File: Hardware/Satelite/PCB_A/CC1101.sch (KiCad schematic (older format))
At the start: 18 parts, among them U2 CC1101RGP, U3 0915BM15A0001E, Y1 26 MHz

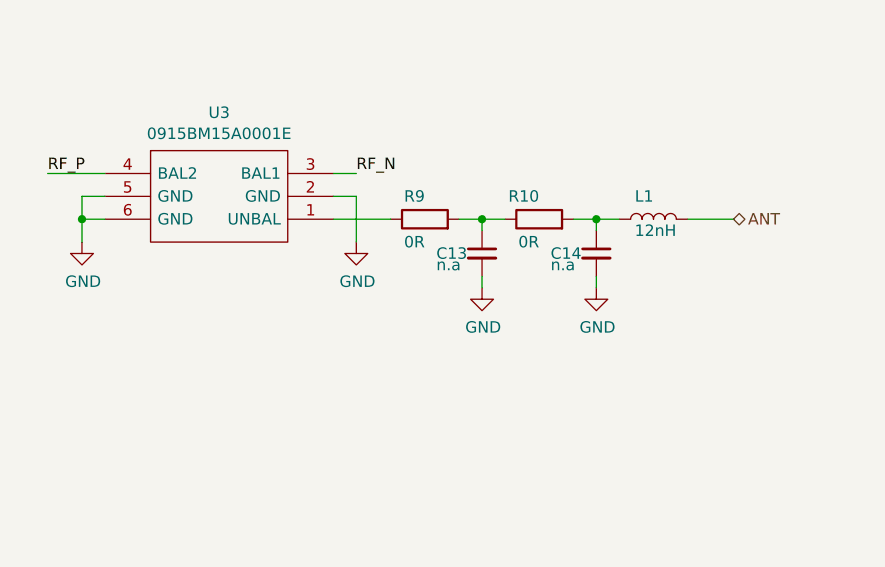
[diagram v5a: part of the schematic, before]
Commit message: Agregado capacitor de bloqueo para el Balun 0896BM15A0001E
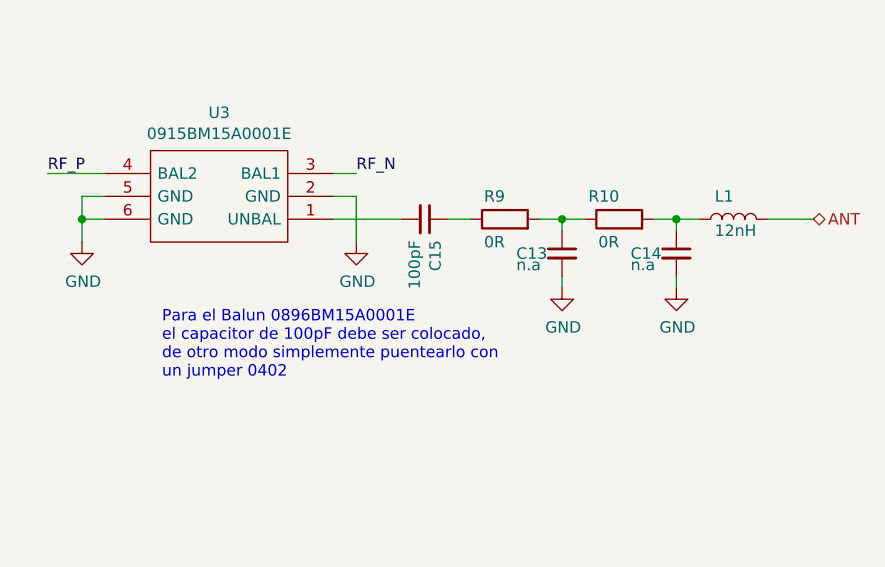
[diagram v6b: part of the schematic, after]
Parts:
- added C15: 100pF, Capacitor_SMD:C_0402_1005Metric, symbol Device:C_Small
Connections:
- net at R9.1: now also C15.1; no longer U3.1 (UNBAL)
- new net: C15.2, U3.1 (UNBAL)
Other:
- note added: "Para el Balun 0896BM15A0001E\nel capacitor de 100pF debe ser colocado,\nde otro modo simplemente puentearlo con\nun jumper 0402"
- moved on the sheet: C13, C14, L1, R10, R9
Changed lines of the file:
@@
 Wire Wire Line
 	3400 4600 3400 4450
-Text HLabel 9300 3400 2    50   BiDi ~ 0
+Text HLabel 9650 3400 2    50   BiDi ~ 0
 ANT
 $Comp
 L Device:C_Small C?
 U 1 1 5BCB61AE
-P 8200 3550
+P 8550 3550
 AR Path="/5B9A8077/5BCB61AE" Ref="C?"  Part="1"
 AR Path="/5BA17F9C/5BCB61AE" Ref="C13"  Part="1"
-F 0 "C13" H 8000 3550 50  0000 L CNN
-F 1 "n.a" H 8000 3500 50  0000 L CNN
-F 2 "Capacitor_SMD:C_0402_1005Metric" H 8200 3550 50  0001 C CNN
-F 3 "~" H 8200 3550 50  0001 C CNN
-	1    8200 3550
+F 0 "C13" H 8350 3550 50  0000 L CNN
+F 1 "n.a" H 8350 3500 50  0000 L CNN
+F 2 "Capacitor_SMD:C_0402_1005Metric" H 8550 3550 50  0001 C CNN
+F 3 "~" H 8550 3550 50  0001 C CNN
+	1    8550 3550
 	1    0    0    -1
 $EndComp
@@
 L Device:R R?
 U 1 1 5BCB61B6
-P 7950 3400
+P 8300 3400
 AR Path="/5B9A8077/5BCB61B6" Ref="R?"  Part="1"
 AR Path="/5BA17F9C/5BCB61B6" Ref="R9"  Part="1"
-F 0 "R9" V 8050 3400 50  0000 L CNN
-F 1 "0R" V 7850 3400 50  0000 L CNN
-F 2 "Resistor_SMD:R_0402_1005Metric" V 7880 3400 50  0001 C CNN
-F 3 "~" H 7950 3400 50  0001 C CNN
-F 4 "RC0402JR-070RL" V 7950 3400 50  0001 C CNN "Manufacturer Part Number"
-	1    7950 3400
+F 0 "R9" V 8400 3400 50  0000 L CNN
+F 1 "0R" V 8200 3400 50  0000 L CNN
+F 2 "Resistor_SMD:R_0402_1005Metric" V 8230 3400 50  0001 C CNN
+F 3 "~" H 8300 3400 50  0001 C CNN
+F 4 "RC0402JR-070RL" V 8300 3400 50  0001 C CNN "Manufacturer Part Number"
+	1    8300 3400
 	0    -1   -1   0
 $EndComp
@@
 L Device:L L?
 U 1 1 5BCB61BE
-P 8950 3400
+P 9300 3400
 AR Path="/5B9A8077/5BCB61BE" Ref="L?"  Part="1"
 AR Path="/5BA17F9C/5BCB61BE" Ref="L1"  Part="1"
-F 0 "L1" V 9050 3400 50  0000 L CNN
-F 1 "12nH" V 8900 3300 50  0000 L CNN
-F 2 "Inductor_SMD:L_0402_1005Metric" H 8950 3400 50  0001 C CNN
-F 3 "https://www.mouser.com/datasheet/2/611/jti-cat-rf-ind-844822.pdf" H 8950 3400 50  0001 C CNN
-F 4 "L-07C12NJV6" V 8950 3400 50  0001 C CNN "Manufacturer Part Number"
-	1    8950 3400
+F 0 "L1" V 9400 3400 50  0000 L CNN
+F 1 "12nH" V 9250 3300 50  0000 L CNN
+F 2 "Inductor_SMD:L_0402_1005Metric" H 9300 3400 50  0001 C CNN
+F 3 "https://www.mouser.com/datasheet/2/611/jti-cat-rf-ind-844822.pdf" H 9300 3400 50  0001 C CNN
+F 4 "L-07C12NJV6" V 9300 3400 50  0001 C CNN "Manufacturer Part Number"
+	1    9300 3400
 	0    -1   -1   0
 $EndComp
@@
 L Device:C_Small C?
 U 1 1 5BCB6272
-P 8700 3550
+P 9050 3550
 AR Path="/5B9A8077/5BCB6272" Ref="C?"  Part="1"
 AR Path="/5BA17F9C/5BCB6272" Ref="C14"  Part="1"
-F 0 "C14" H 8500 3550 50  0000 L CNN
-F 1 "n.a" H 8500 3500 50  0000 L CNN
-F 2 "Capacitor_SMD:C_0402_1005Metric" H 8700 3550 50  0001 C CNN
-F 3 "~" H 8700 3550 50  0001 C CNN
-	1    8700 3550
-	1    0    0    -1
-$EndComp
-Wire Wire Line
-	8100 3400 8200 3400
-Wire Wire Line
-	8200 3450 8200 3400
-Connection ~ 8200 3400
-Wire Wire Line
-	8200 3400 8300 3400
-Wire Wire Line
-	8600 3400 8700 3400
-Wire Wire Line
-	8700 3450 8700 3400
-Connection ~ 8700 3400
-Wire Wire Line
-	8700 3400 8800 3400
-Wire Wire Line
-	7550 3400 7800 3400
+F 0 "C14" H 8850 3550 50  0000 L CNN
+F 1 "n.a" H 8850 3500 50  0000 L CNN
+F 2 "Capacitor_SMD:C_0402_1005Metric" H 9050 3550 50  0001 C CNN
+F 3 "~" H 9050 3550 50  0001 C CNN
+	1    9050 3550
+	1    0    0    -1
+$EndComp
+Wire Wire Line
+	8450 3400 8550 3400
+Wire Wire Line
+	8550 3450 8550 3400
+Connection ~ 8550 3400
+Wire Wire Line
+	8550 3400 8650 3400
+Wire Wire Line
+	8950 3400 9050 3400
+Wire Wire Line
+	9050 3450 9050 3400
+Connection ~ 9050 3400
+Wire Wire Line
+	9050 3400 9150 3400
 $Comp
 L power:GND #PWR?
 U 1 1 5BCB6282
-P 8200 3700
+P 8550 3700
 AR Path="/5B9A8077/5BCB6282" Ref="#PWR?"  Part="1"
 AR Path="/5BA17F9C/5BCB6282" Ref="#PWR044"  Part="1"
-F 0 "#PWR044" H 8200 3450 50  0001 C CNN
-F 1 "GND" H 8205 3527 50  0000 C CNN
-F 2 "" H 8200 3700 50  0001 C CNN
-F 3 "" H 8200 3700 50  0001 C CNN
-	1    8200 3700
+F 0 "#PWR044" H 8550 3450 50  0001 C CNN
+F 1 "GND" H 8555 3527 50  0000 C CNN
+F 2 "" H 8550 3700 50  0001 C CNN
+F 3 "" H 8550 3700 50  0001 C CNN
+	1    8550 3700
 	1    0    0    -1
 $EndComp
@@
 L power:GND #PWR?
 U 1 1 5BCB6288
-P 8700 3700
+P 9050 3700
 AR Path="/5B9A8077/5BCB6288" Ref="#PWR?"  Part="1"
 AR Path="/5BA17F9C/5BCB6288" Ref="#PWR045"  Part="1"
-F 0 "#PWR045" H 8700 3450 50  0001 C CNN
-F 1 "GND" H 8705 3527 50  0000 C CNN
-F 2 "" H 8700 3700 50  0001 C CNN
-F 3 "" H 8700 3700 50  0001 C CNN
-	1    8700 3700
-	1    0    0    -1
-$EndComp
-Wire Wire Line
-	8200 3650 8200 3700
-Wire Wire Line
-	8700 3650 8700 3700
+F 0 "#PWR045" H 9050 3450 50  0001 C CNN
+F 1 "GND" H 9055 3527 50  0000 C CNN
+F 2 "" H 9050 3700 50  0001 C CNN
+F 3 "" H 9050 3700 50  0001 C CNN
+	1    9050 3700
+	1    0    0    -1
+$EndComp
+Wire Wire Line
+	8550 3650 8550 3700
+Wire Wire Line
+	9050 3650 9050 3700
 Wire Wire Line
 	7550 3300 7650 3300
@@
 	7650 3300 7650 3500
 Wire Wire Line
-	9100 3400 9300 3400
+	9450 3400 9650 3400
 Wire Wire Line
 	2800 3150 2600 3150
@@
 L Device:R R?
 U 1 1 5BCB6303
-P 8450 3400
+P 8800 3400
 AR Path="/5B9A8077/5BCB6303" Ref="R?"  Part="1"
 AR Path="/5BA17F9C/5BCB6303" Ref="R10"  Part="1"
-F 0 "R10" V 8550 3400 50  0000 L CNN
-F 1 "0R" V 8350 3400 50  0000 L CNN
-F 2 "Resistor_SMD:R_0402_1005Metric" V 8380 3400 50  0001 C CNN
-F 3 "~" H 8450 3400 50  0001 C CNN
-F 4 "RC0402JR-070RL" V 8450 3400 50  0001 C CNN "Manufacturer Part Number"
-	1    8450 3400
+F 0 "R10" V 8900 3400 50  0000 L CNN
+F 1 "0R" V 8700 3400 50  0000 L CNN
+F 2 "Resistor_SMD:R_0402_1005Metric" V 8730 3400 50  0001 C CNN
+F 3 "~" H 8800 3400 50  0001 C CNN
+F 4 "RC0402JR-070RL" V 8800 3400 50  0001 C CNN "Manufacturer Part Number"
+	1    8800 3400
 	0    -1   -1   0
 $EndComp
@@
 Wire Wire Line
 	3300 4600 3400 4600
+$Comp
+L Device:C_Small C?
+U 1 1 5E1DA171
+P 7950 3400
+AR Path="/5B9997DB/5E1DA171" Ref="C?"  Part="1"
+AR Path="/5B9A8077/5E1DA171" Ref="C?"  Part="1"
+AR Path="/5BA17F9C/5E1DA171" Ref="C15"  Part="1"
+F 0 "C15" H 8042 3446 50  0000 L CNN
+F 1 "100pF" H 8042 3355 50  0000 L CNN
+F 2 "Capacitor_SMD:C_0402_1005Metric" H 7950 3400 50  0001 C CNN
+F 3 "~" H 7950 3400 50  0001 C CNN
+F 4 "NP0" H 7950 3400 50  0001 C CNN "Dielectric"
+F 5 "25V" H 7950 3400 50  0001 C CNN "Voltage"
+F 6 "885012005046" H 7950 3400 50  0001 C CNN "Manufacturer Part Number"
+	1    7950 3400
+	0    1    1    0
+$EndComp
+Wire Wire Line
+	7550 3400 7850 3400
+Wire Wire Line
+	8050 3400 8150 3400
+Text Notes 6800 4100 0    50   ~ 0
+Para el Balun 0896BM15A0001E\nel capacitor de 100pF debe ser colocado,\nde otro modo simplemente puentearlo con\nun jumper 0402
 $EndSCHEMATC
